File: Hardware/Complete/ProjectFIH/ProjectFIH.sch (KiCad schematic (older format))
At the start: 62 parts, among them J1 Conn_01x02_Male, J2 Heater, J3 Payload, Q1 2N7002, Q2 2N7002, Q3 IRLZ44N, U1 74HC04, U2 LM158, U3 74HC4017, U4 74HC02, U5 74HC08, U6 LM22675-5.0, U7 LM2576S-ADJ

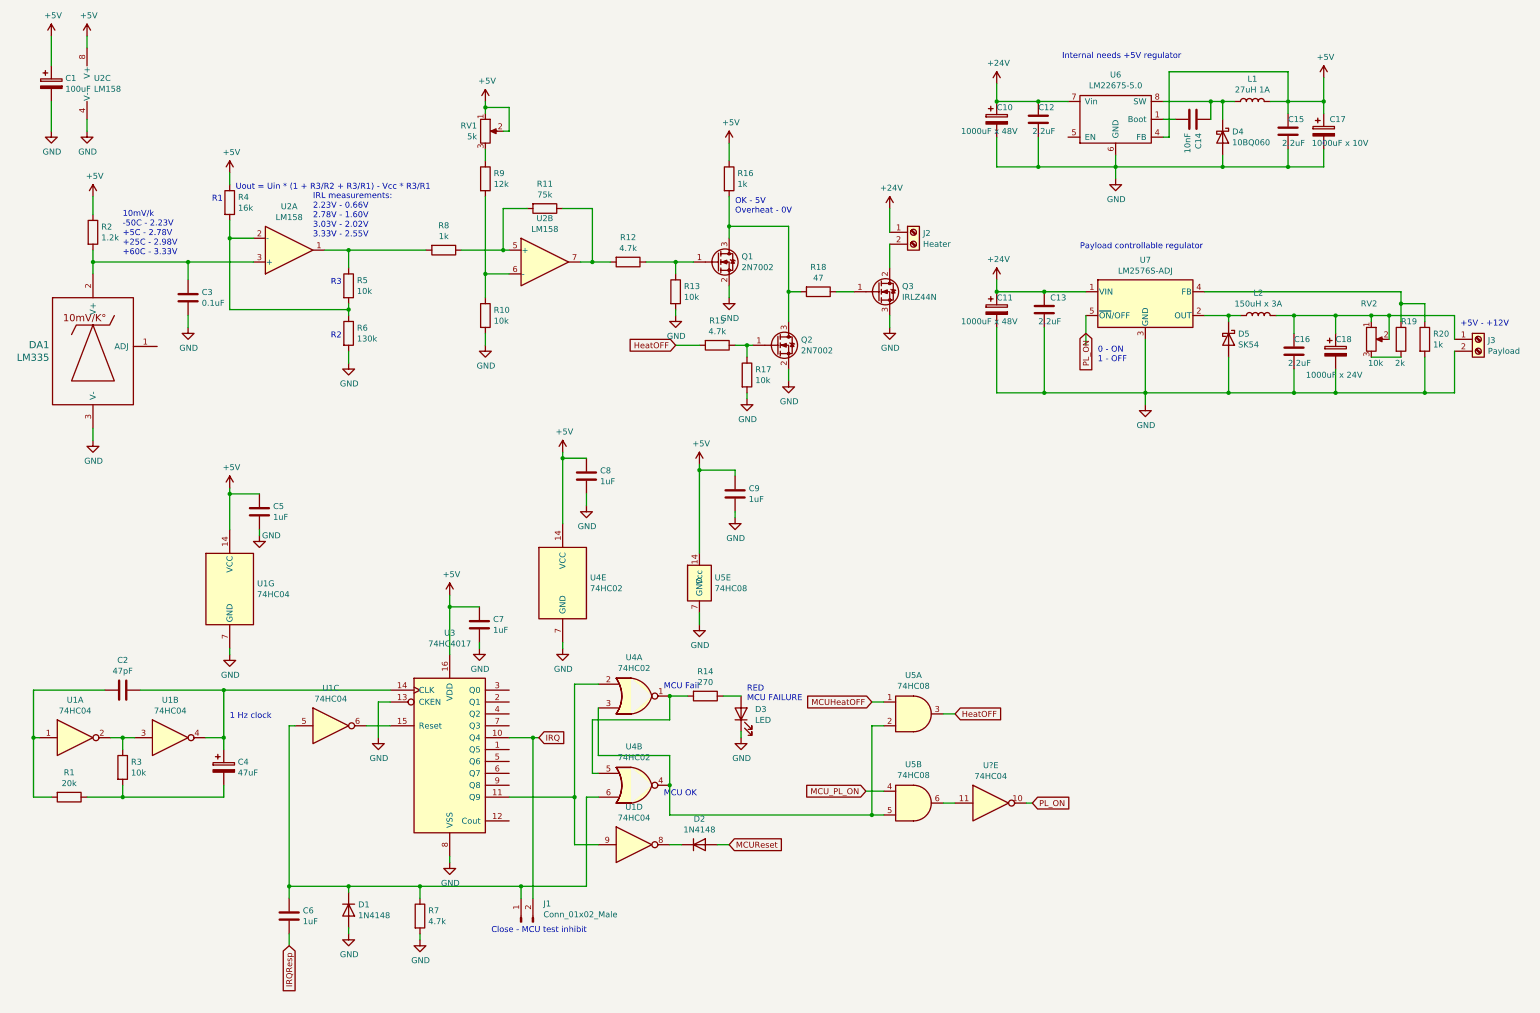
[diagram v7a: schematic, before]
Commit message: Fixed incorrect counter reset.
Ready to add MCU and start PCB tracing
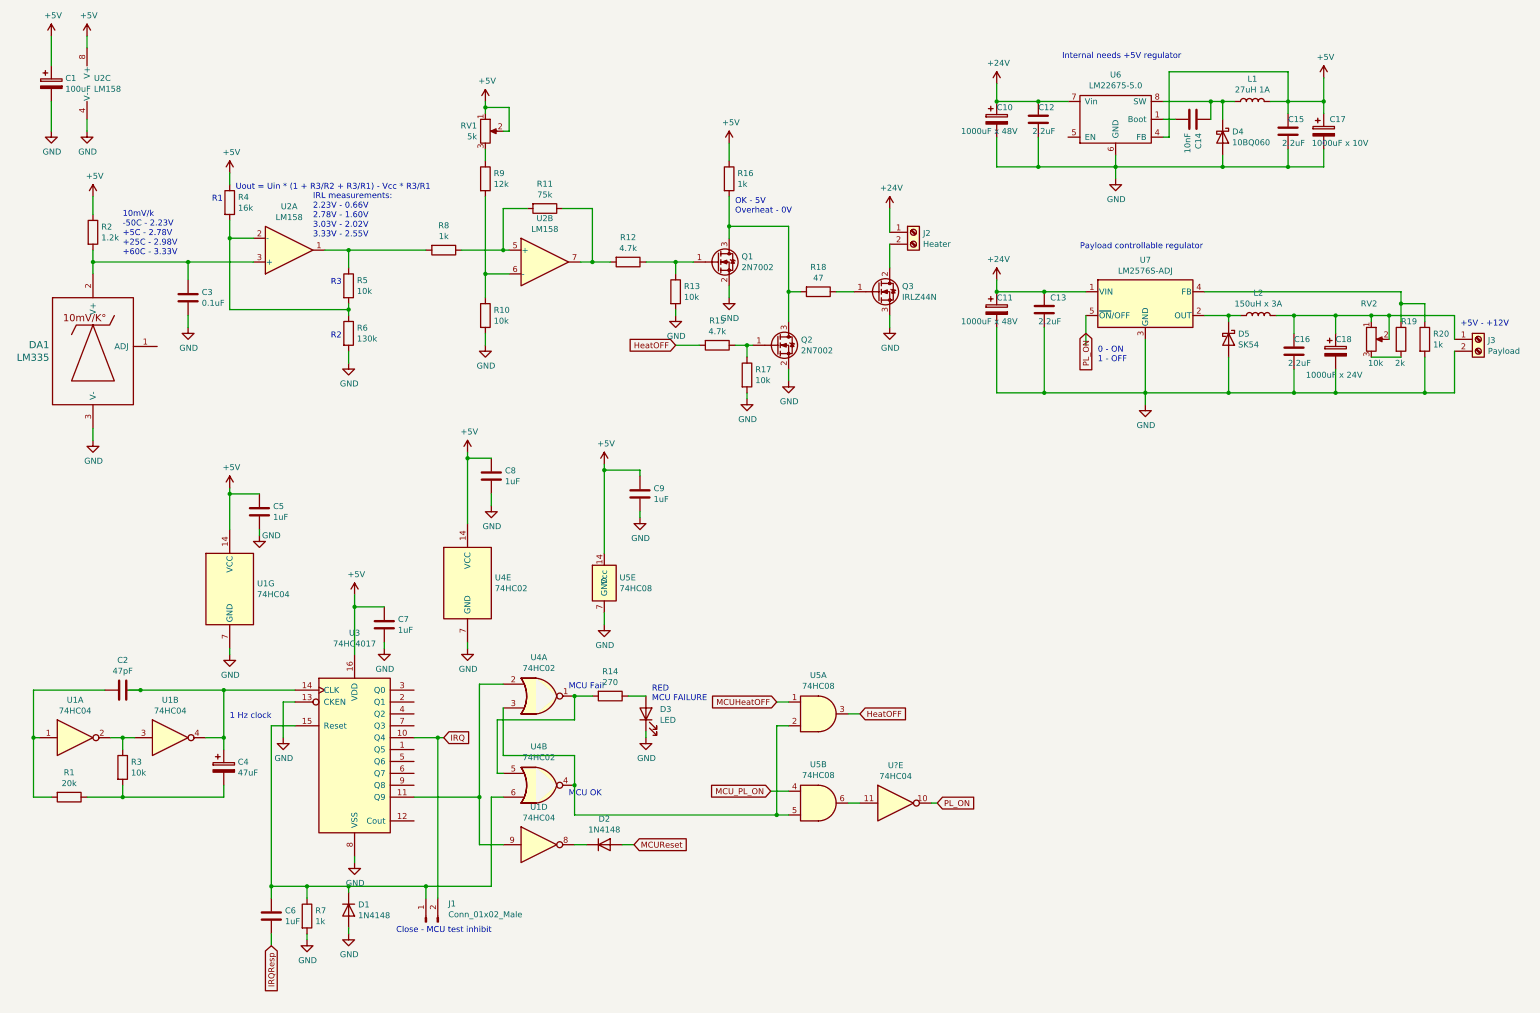
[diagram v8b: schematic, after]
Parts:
- removed unit 3 of U1
- R7: value 4.7k -> 1k
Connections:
- net at U3.15 (Reset): now also C6.1, D1.1 (K), J1.1 (Pin_1), R7.1, U4.6
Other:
- moved on the sheet: C6, C7, C8, C9, D2, D3, J1, R14, R7, U1D, U3, U4A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
